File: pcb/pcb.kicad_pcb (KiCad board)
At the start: 2 copper layers, 163.7 x 99.9 mm, 51 parts, among them J1 N!N, J2 Conn_01x02_Socket, J3 Conn_01x12_Socket, J4 Display_nice-view, J5 Conn_01x12_Socket, J6 Conn_01x12_Socket, J7 Conn_01x12_Socket, SW1 Switch, SW10 Switch, SW11 Switch, SW12 Switch, SW13 Switch, SW14 Switch, SW15 Switch, SW16 Switch, SW17 Switch, SW18 Switch, SW19 Switch, SW2 Switch, SW20 Switch, SW21 SW_Push, SW22 SW_SPDT, SW3 Switch, SW4 Switch, SW5 Switch, SW6 Switch, SW7 Switch, SW8 Switch, SW9 Switch

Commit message: final pcb
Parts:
- added J8: Conn_01x12_Socket, Connector_FFC-FPC:TE_1-84952-2_1x12-1MP_P1.0mm_Horizontal, B.Cu at (160.0, 90.1)
- added J9: Conn_01x12_Socket, Connector_FFC-FPC:TE_1-84952-2_1x12-1MP_P1.0mm_Horizontal, F.Cu at (160.0, 90.1)
- J4: value Display_nice-view -> nice!view
- J6: moved to B.Cu
- J7: moved to F.Cu
- moved J6 7.28 mm to (165.0, 87.5), turned to -72 degrees
- moved J7 7.28 mm to (165.0, 87.5), turned to 108 degrees
- moved J3 1.41 mm to (155.0, 91.5)
- moved J5 1.41 mm to (155.0, 91.5)
- turned D19 to 170 degrees
- turned D20 to 160 degrees
- turned D14 to 180 degrees
- turned D15 to 180 degrees
- turned D3 to 180 degrees
- turned D17 to 180 degrees
- turned D5 to 180 degrees
- turned D18 to 180 degrees
- turned D12 to 180 degrees
- turned D9 to 180 degrees
- turned D4 to 180 degrees
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- renumbered D20 to D1, D12 to D11, D13 to D12, D14 to D13, D15 to D14, D16 to D15, D5 to D16, D11 to D17, D17 to D18, D18 to D19, D1 to D2, D19 to D20, D2 to D3, D3 to D4, D4 to D5, SW20 to SW1, SW12 to SW11, SW13 to SW12, SW14 to SW13, SW15 to SW14, SW16 to SW15, SW5 to SW16, SW11 to SW17, SW17 to SW18, SW18 to SW19, SW1 to SW2, SW19 to SW20, SW2 to SW3, SW3 to SW4, SW4 to SW5
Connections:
- D1 pad 1: row3 -> row0
- D15 pad 1: row3 -> row2
- D16 pad 1: row0 -> row3
- D17 pad 1: row2 -> row3
- J1 pad 1: (no net) -> CS
- J1 pad 10: col3_r -> col2_r
- J1 pad 11: col2_r -> col1_r
- J1 pad 12: col1_r -> col0_r
- J1 pad 13: col0_r -> row2
- J1 pad 14: (no net) -> row1
- J1 pad 15: unconnected-(J1-101-Pad15) -> row0
- J1 pad 16: unconnected-(J1-102-Pad16) -> col4
- J1 pad 17: unconnected-(J1-107-Pad17) -> col3
- J1 pad 18: (no net) -> col2
- J1 pad 19: row2 -> col1
- J1 pad 2: MOSI -> row4
- J1 pad 20: row1 -> col0
- J1 pad 21: row0 -> +3.3V
- J1 pad 22: col4 -> RST
- J1 pad 23: col3 -> GND
- J1 pad 24: col2 -> BAT
- J1 pad 3: row4 -> GND
- J1 pad 5: GND -> SCK
- J1 pad 7: SCK -> row3
- J1 pad 8: row3 -> col4_r
- J1 pad 9: col4_r -> col3_r
- S2 pad 1: col0_r -> col0
- S2 pad 2: col4_r -> col4
- S2 pad 3: col2_r -> col2
- S2 pad 4: col1_r -> col1
- S2 pad 6: col3_r -> col3
- SW1 pad 2: col4 -> col0
- SW11 pad 2: col1 -> col0
- SW12 pad 2: col2 -> col1
- SW13 pad 2: col3 -> col2
- SW14 pad 2: col4 -> col3
- SW15 pad 2: col0 -> col4
- SW16 pad 2: col4 -> col0
- SW17 pad 2: col0 -> col1
- SW18 pad 2: col1 -> col2
- SW19 pad 2: col2 -> col3
- SW2 pad 2: col0 -> col1
- SW20 pad 2: col3 -> col4
- SW3 pad 2: col1 -> col2
- SW4 pad 2: col2 -> col3
- SW5 pad 2: col3 -> col4
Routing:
- net col1: track 0.00 -> 316.8 mm, vias 0 -> 7
- net col0: track 0.00 -> 314.6 mm, vias 0 -> 7
- net col3: track 0.00 -> 274.2 mm, vias 0 -> 8
- net col2: track 0.00 -> 261.3 mm, vias 0 -> 7
- net col4: track 0.00 -> 253.5 mm, vias 0 -> 7
- net row3: track 0.00 -> 246.5 mm, vias 0 -> 7
- net row4: track 0.00 -> 227.4 mm, vias 0 -> 2
- net row0: track 0.00 -> 192.5 mm, vias 0 -> 6
- net row1: track 0.00 -> 178.7 mm, vias 0 -> 6
- net row2: track 0.00 -> 168.2 mm, vias 0 -> 7
- net GND: track 0.00 -> 164.0 mm, vias 0 -> 1
- net BAT: track 0.00 -> 154.9 mm, vias 0 -> 2
- net BATIN: track 0.00 -> 93.4 mm
- net +3.3V: track 0.00 -> 76.8 mm
- net CS: track 0.00 -> 63.7 mm
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- removed copper zone on B.Cu, net (none)
- removed copper zone on F.Cu, net (none)
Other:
- outline, holes or cut-outs redrawn
- board text added: "+"
- board text added: "-"
- board text added: "BATTERY"
- board text added: "D U"
- board text added: "E T"
- board text added: "H"
- board text added: "LEFT"
- board text added: "OFF"
- board text added: "ON"
- board text added: "RESET"
- board text added: "RIGHT"
- board text added: "chip facing PCB"
- board text added: "https://github.com/zzeneg/duet"
- board text added: "nice!nano"

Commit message: small updates to silkscreen and logo
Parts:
- added G***: LOGO, zzkeeb:Logo_fusion-dance-left, F.Cu at (192.2, 97.4)
- added G***: LOGO, zzkeeb:Logo_fusion-dance-right, B.Cu at (192.2, 97.3)
- added REF**: Hole_M2-TH, zzkeeb:Hole_M2-TH, F.Cu at (150.4, 98.6)
- added REF**: Hole_M2-TH, zzkeeb:Hole_M2-TH, F.Cu at (105.1, 98.9)
- added REF**: Hole_M2-TH, zzkeeb:Hole_M2-TH, F.Cu at (48.6, 106.9)
- added REF**: Hole_M2-TH, zzkeeb:Hole_M2-TH, F.Cu at (137.5, 45.1)
- added REF**: Hole_M2-TH, zzkeeb:Hole_M2-TH, F.Cu at (170.2, 36.7)
- added REF**: Hole_M2-TH, zzkeeb:Hole_M2-TH, F.Cu at (84.6, 44.1)
- added REF**: Hole_M2-TH, zzkeeb:Hole_M2-TH, F.Cu at (48.6, 63.1)
- added REF**: Hole_M2-TH, zzkeeb:Hole_M2-TH, F.Cu at (185.5, 101.2)
- moved J3 1.08 mm to (155.1, 90.4)
- moved J5 1.08 mm to (155.1, 90.4)
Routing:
- net row2: track 168.2 -> 163.2 mm
- net col4: track 253.5 -> 251.8 mm
- net row3: track 246.5 -> 248.2 mm
- net col0: track 314.6 -> 312.9 mm
- net BAT: track 154.9 -> 153.9 mm
- net GND: track 164.0 -> 163.0 mm
- net row1: track 178.7 -> 177.9 mm
- net col3: track 274.2 -> 273.4 mm
- net row0: track 192.5 -> 192.0 mm
- net col2: track 261.3 -> 260.8 mm
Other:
- outline, holes or cut-outs redrawn
- board text added: "v0.1"

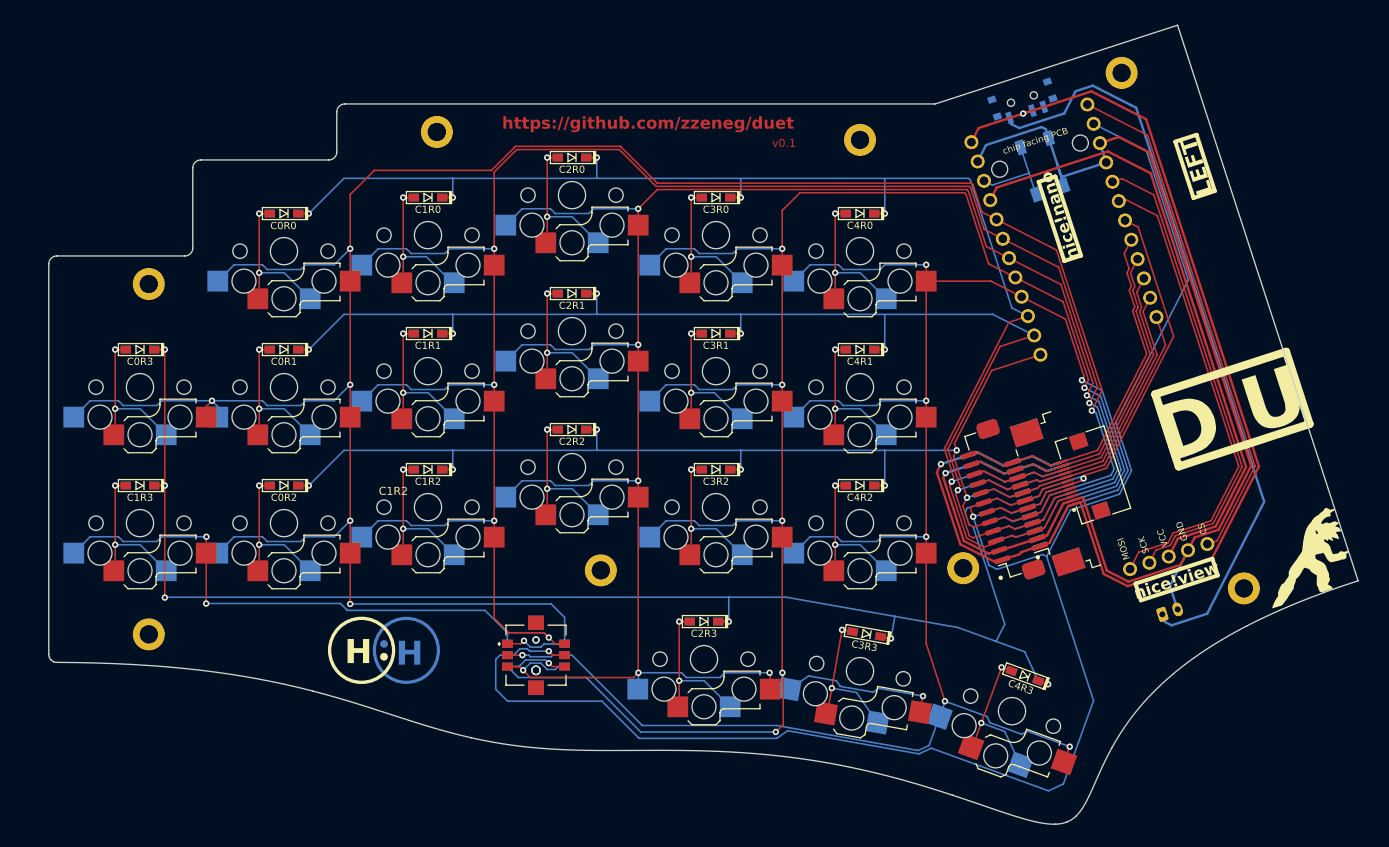
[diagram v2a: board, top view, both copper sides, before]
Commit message: improve niceview pin mappings
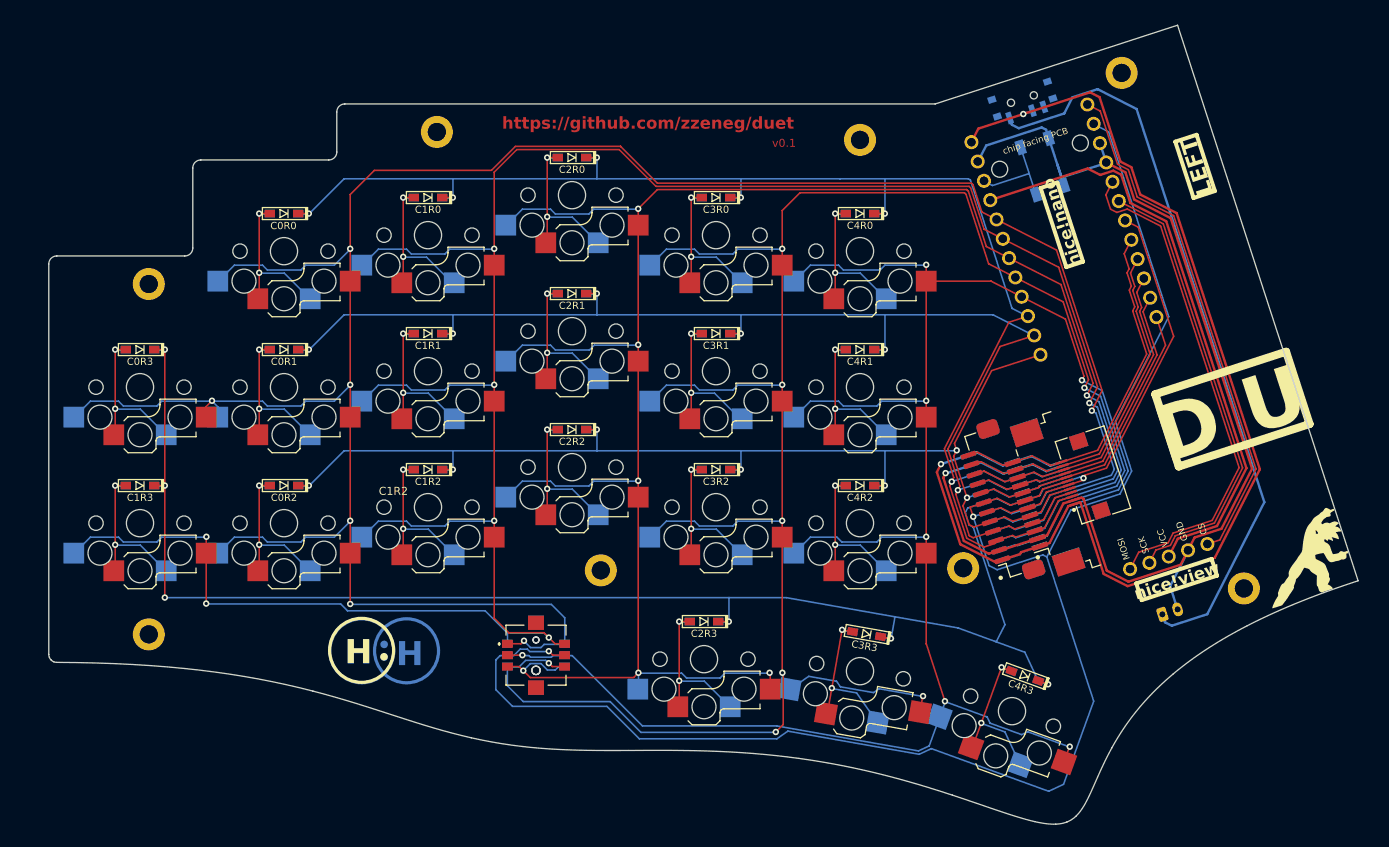
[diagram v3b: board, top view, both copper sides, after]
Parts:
- H1, H2, H3, H4, H5, H6, H7, H8: renamed from REF**; value Hole_M2-TH -> MountingHole
- J4: value nice!view -> Display_nice-view
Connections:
- J1 pad 5: SCK -> MOSI
- J1 pad 6: MOSI -> SCK
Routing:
- net GND: track 163.0 -> 158.3 mm
- net MOSI: track 58.5 -> 62.5 mm
- net SCK: track 59.4 -> 56.2 mm
- net row4: track 227.8 -> 224.8 mm
- net +3.3V: track 76.8 -> 74.3 mm
- net col3: track 273.4 -> 275.0 mm
- net BATIN: track 93.4 -> 92.8 mm
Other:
- board text added: "nice!view"

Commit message: rotate alps 5way footprint to correct position
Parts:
- turned S1 to 90 degrees
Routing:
- net row4: track 224.8 -> 219.0 mm
- net col0: track 312.9 -> 307.7 mm
- net col1: track 316.5 -> 312.4 mm
- net col2: track 260.8 -> 257.3 mm
- net col3: track 275.0 -> 271.6 mm
- net col4: track 251.9 -> 255.2 mm
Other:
- board text added: "v0.2"
- board text removed: "v0.1"

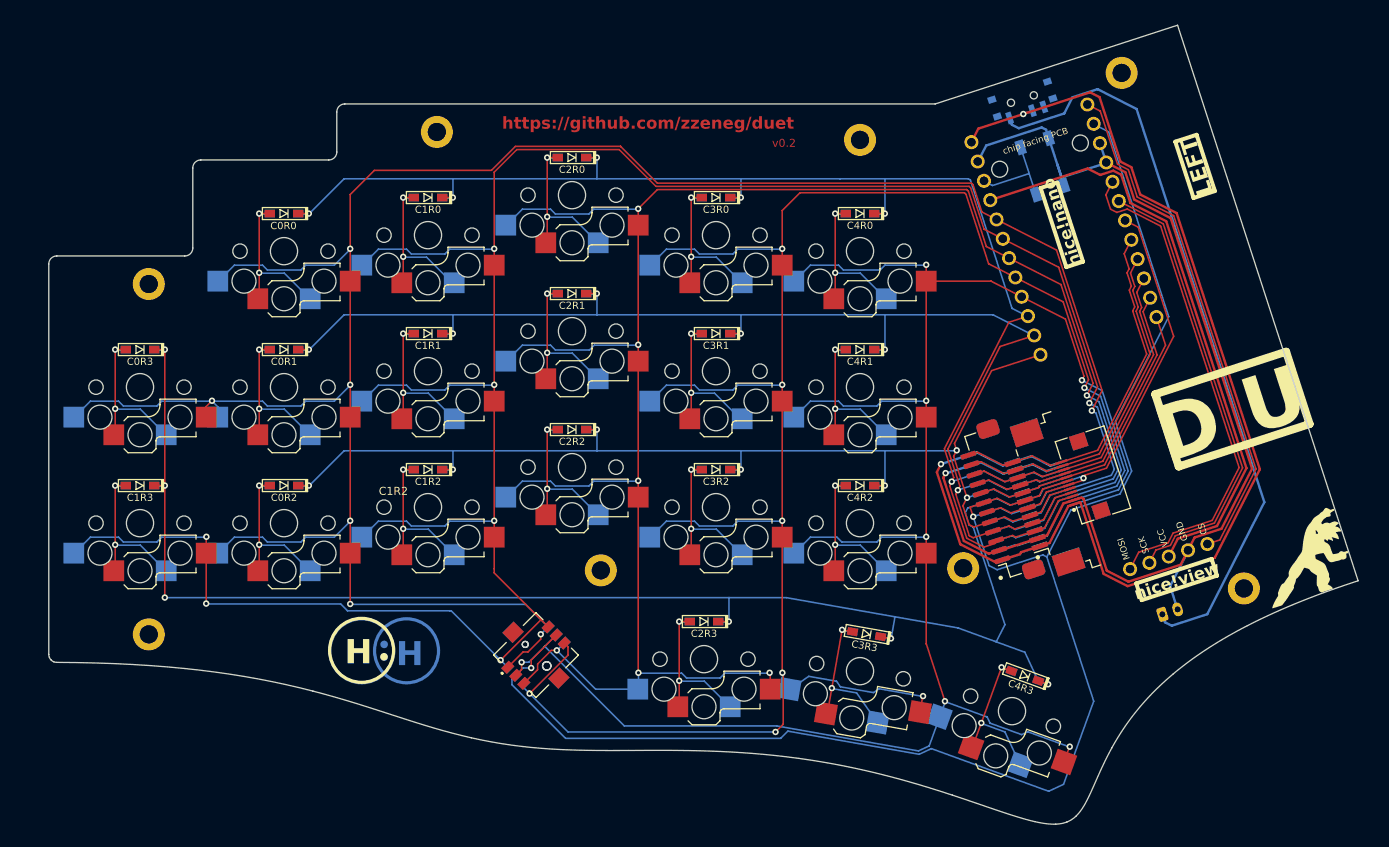
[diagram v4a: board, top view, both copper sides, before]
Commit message: simplify pcb, reduce cover size
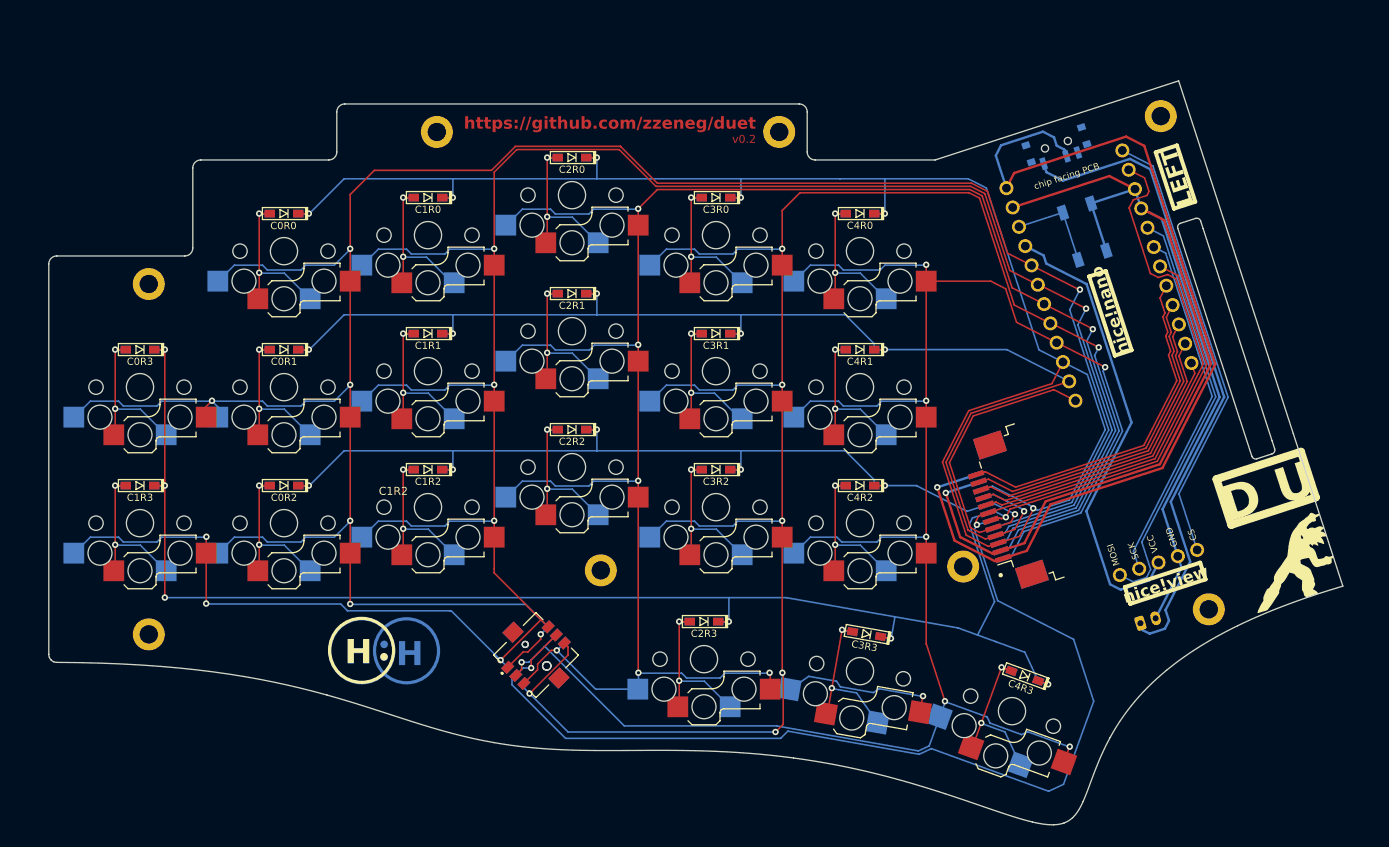
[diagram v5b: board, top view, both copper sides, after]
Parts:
- removed J3, J5: Conn_01x12_Socket, zzkeeb:Connector_JST-1x12-P1.25mm
- removed J6, J7: Conn_01x12_Socket, zzkeeb:Connector_VIK-horizontal-keyboard
- moved H3 10.2 mm to (127.4, 44.1)
- moved SW21 9.73 mm to (165.6, 56.6)
- moved H4 7.29 mm to (175.1, 42.1)
- moved J1 7.22 mm to (167.0, 60.8)
- moved SW22 7.12 mm to (162.2, 46.0)
- moved H8 5.10 mm to (181.1, 103.8)
- moved J8 4.83 mm to (155.4, 91.6)
- moved J9 4.83 mm to (155.4, 91.6)
- moved J2 2.96 mm to (172.5, 105.5)
- moved G*** 1.95 mm to (190.4, 97.9)
- moved G*** 1.94 mm to (190.3, 98.0)
- moved J4 1.48 mm to (169.7, 82.2)
- moved H7 0.20 mm to (150.4, 98.4)
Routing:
- net BAT: track 153.9 -> 121.6 mm, vias 2 -> 1
- net row4: track 219.0 -> 192.9 mm
- net row0: track 192.0 -> 211.0 mm
- net +3.3V: track 74.3 -> 57.3 mm
- net row1: track 177.9 -> 162.7 mm
- net row3: track 248.3 -> 233.1 mm
- net row2: track 163.2 -> 148.2 mm, vias 7 -> 6
- net BATIN: track 92.8 -> 80.8 mm
- net SCK: track 56.2 -> 44.5 mm
- net MOSI: track 62.5 -> 52.1 mm
- net CS: track 63.9 -> 55.6 mm
- net GND: track 158.3 -> 163.5 mm
- net col4: track 255.2 -> 252.8 mm
- net col0_r: track 37.0 -> 34.9 mm
- net col0: track 307.7 -> 305.7 mm
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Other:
- board size 163.7 x 99.9 mm -> 161.8 x 93 mm

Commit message: small updates
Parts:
- D1, D10, D11, D12, D13, D14, D15, D16, D17, D18, D19, D2, D20, D3, D4, D5, D6, D7, D8, D9: footprint zzkeeb:Diode_1N4148-SOD123-reversible -> zzkeeb:Diode_1N4148-SOD123-reversible-flip3d
- J8, J9: footprint Connector_FFC-FPC:TE_1-84952-2_1x12-1MP_P1.0mm_Horizontal -> zzkeeb:Connector_FFC-12pin-1mm-horizontal
- moved J9 1.00 mm to (154.5, 91.9)
- moved J8 1.00 mm to (154.5, 91.9)
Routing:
- net row1: track 162.7 -> 165.7 mm
- net row2: track 148.2 -> 151.0 mm
- net row0: track 211.0 -> 213.7 mm
- net row3: track 233.1 -> 234.4 mm
- net RST: track 12.0 -> 12.6 mm
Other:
- outline, holes or cut-outs redrawn
- board text removed: "LEFT"
- board text removed: "RIGHT"
